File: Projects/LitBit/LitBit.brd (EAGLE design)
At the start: 48.8 x 38.1 mm, 87 parts, among them J1 Battery, Q2 CSTCR6M00G53Z, U1 24FC1025, U2 RTC_MCP7940N8-MSOP, U3 ADXL345, U4 UP_ATMEGA32U4-AU, U5 S-1335J33-M5T1U3, U6 nRF8001, U7 MCP73831, Y1 16.0000 MHz, Y2 32.7680 kHz, Y3 32.7680 kHz

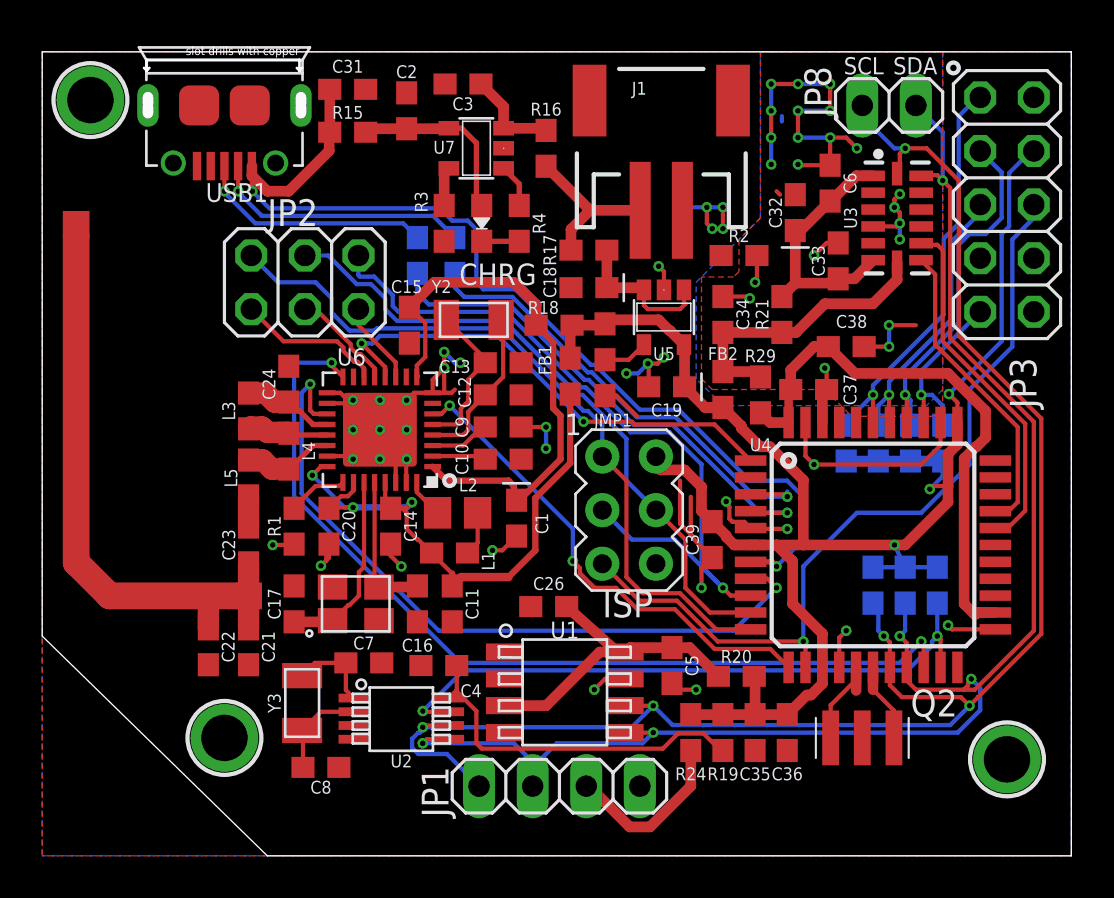
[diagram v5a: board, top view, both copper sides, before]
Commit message: remove dimension layer text
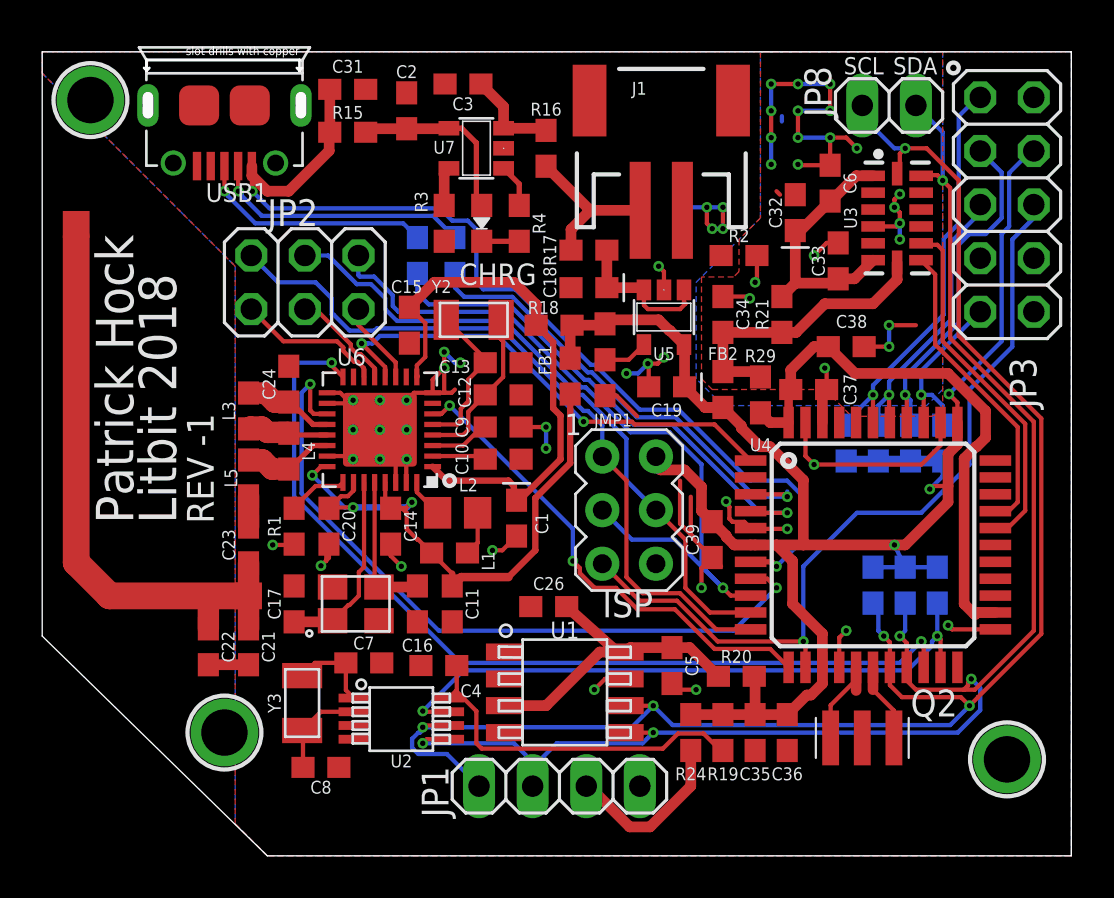
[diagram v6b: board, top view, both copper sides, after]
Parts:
- moved U$8 0.25 mm to (8.64, 5.84)
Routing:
- net GND: track 74.3 -> 76.2 mm
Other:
- board text added: "Litbit 2018"
- board text added: "Patrick Hock"
- board text added: "REV -1"
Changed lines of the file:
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@@
 <circle x="43.18" y="37.338" radius="0.254" width="0.2032" layer="21"/>
 <circle x="19.304" y="17.78" radius="0.254" width="0.2032" layer="21"/>
-<dimension x1="0.254" y1="38.1" x2="48.768" y2="38.1" x3="24.511" y3="41.656" textsize="1.778" layer="20" unit="inch"/>
 <wire x1="48.768" y1="0" x2="48.768" y2="38.1" width="0" layer="20"/>
 <wire x1="48.768" y1="38.1" x2="0" y2="38.1" width="0" layer="20"/>
@@
 <wire x1="0" y1="10.414" x2="10.668" y2="0" width="0" layer="20"/>
 <wire x1="10.668" y1="0" x2="48.768" y2="0" width="0" layer="20"/>
+<text x="4.318" y="15.748" size="1.778" layer="21" rot="R90">Patrick Hock</text>
+<text x="6.35" y="15.748" size="1.778" layer="21" rot="R90">Litbit 2018</text>
+<text x="8.128" y="15.748" size="1.27" layer="21" rot="R90">REV -1</text>
 </plain>
 <attributes>
@@
 <attribute name="VALUE" x="32.385" y="14.986" size="0.6096" layer="27" rot="R90" align="top-center"/>
 </element>
-<element name="U$8" library="microbuilder" package="MOUNTINGHOLE_2.0_PLATED" value="MOUNTINGHOLE2.0" x="8.636" y="5.588"/>
+<element name="U$8" library="microbuilder" package="MOUNTINGHOLE_2.0_PLATED" value="MOUNTINGHOLE2.0" x="8.636" y="5.842"/>
 </elements>
 <signals>
@@
 <vertex x="48.768" y="38.1"/>
 <vertex x="0" y="38.1"/>
-<vertex x="0" y="0"/>
+<vertex x="0" y="37.084"/>
+<vertex x="6.604" y="30.48"/>
+<vertex x="9.144" y="27.94"/>
+<vertex x="9.144" y="1.524"/>
+<vertex x="10.668" y="0"/>
 <vertex x="48.768" y="0"/>
 </polygon>
 <contactref element="R2" pad="1"/>
 <polygon width="0.254" layer="1" rank="6">
-<vertex x="0" y="0"/>
+<vertex x="10.668" y="0"/>
+<vertex x="9.144" y="1.524"/>
+<vertex x="9.144" y="27.94"/>
+<vertex x="0" y="37.084"/>
 <vertex x="0" y="38.1"/>
 <vertex x="48.768" y="38.1"/>
@@
 <wire x1="16.51" y1="14.224" x2="17.018" y2="13.716" width="0.2032" layer="1"/>
 <via x="17.018" y="13.716" extent="1-16" drill="0.254"/>
+<wire x1="9.779" y1="9.056" x2="7.874" y2="9.056" width="0.508" layer="1"/>
 </signal>
 <signal name="3.3V">
@@
 </signal>
 </signals>
+<errors>
+</errors>
 </board>
 </drawing>
